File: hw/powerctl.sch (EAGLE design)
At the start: 12 parts, among them J1 MA02-1, J3 JST-XH-3P, J4 MA02-1

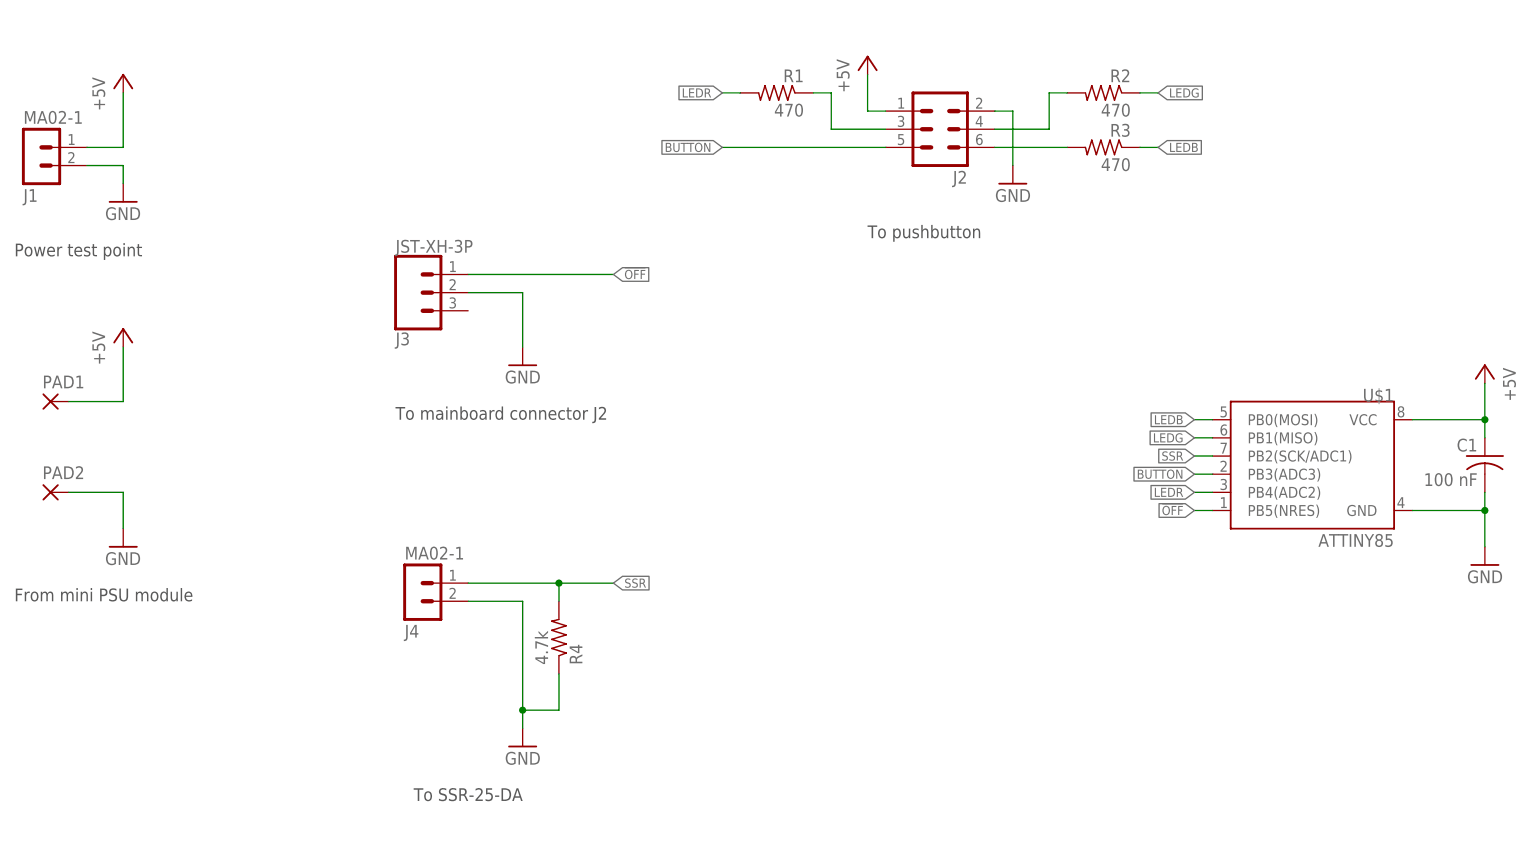
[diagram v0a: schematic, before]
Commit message: hw: update hardware, including warning about JST jumper cable
Update the hardware schematic to indicate the pinout for the button
connector, and note the oddness with the apparent commonness(???) of
JST jumper cable crossover cables.
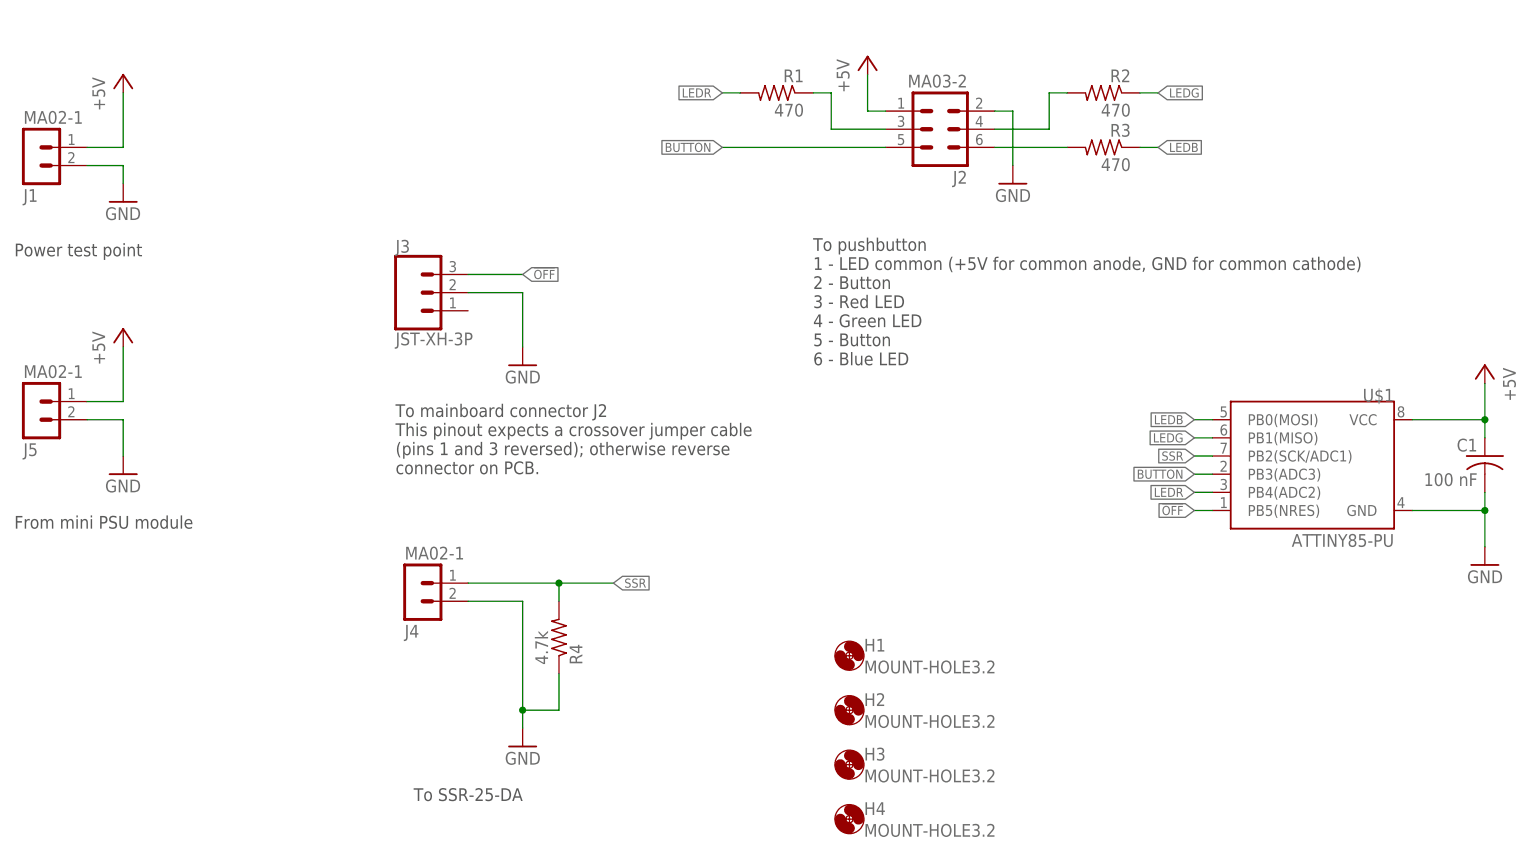
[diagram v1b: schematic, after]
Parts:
- removed PAD1, PAD2: (no value), wirepad:2,15/1,0
- added H1, H2, H3, H4: MOUNT-HOLE3.2, holes:MOUNT-HOLE3.2
- added J5: MA02-1, con-lstb:MA02-1
- J2: value (none) -> MA03-2
- U$1: value ATTINY85 -> ATTINY85-PU
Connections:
- net !OFF: now also J3.3; no longer J3.1
- net +5V: now also J5.1; no longer PAD1.P
- net GND: now also J5.2; no longer PAD2.P
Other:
- note added: "To mainboard connector J2 This pinout expects a crossover jumper cable (pins 1 and 3 reversed); otherwise reverse connector on PCB."
- note added: "To pushbutton 1 - LED common (+5V for common anode, GND for common cathode) 2 - Button 3 - Red LED 4 - Green LED 5 - Button 6 - Blue LED"
- note removed: "To mainboard connector J2"
- note removed: "To pushbutton"
- moved on the sheet: J3
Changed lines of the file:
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@@
 <parts>
 <part name="FRAME1" library="frames" deviceset="FRAME_A_L" device=""/>
-<part name="U$1" library="SparkFun" deviceset="ATTINY13" device="DIP" value="ATTINY85"/>
-<part name="PAD1" library="wirepad" deviceset="2,15/1,0" device=""/>
-<part name="PAD2" library="wirepad" deviceset="2,15/1,0" device=""/>
+<part name="U$1" library="SparkFun" deviceset="ATTINY13" device="DIP" value="ATTINY85-PU"/>
 <part name="P+1" library="supply1" deviceset="+5V" device=""/>
 <part name="GND1" library="supply1" deviceset="GND" device=""/>
@@
 <part name="J1" library="con-lstb" deviceset="MA02-1" device=""/>
 <part name="J4" library="con-lstb" deviceset="MA02-1" device=""/>
-<part name="J2" library="con-lstb" deviceset="MA03-2" device=""/>
+<part name="J2" library="con-lstb" deviceset="MA03-2" device="" value="MA03-2"/>
 <part name="P+4" library="supply1" deviceset="+5V" device=""/>
 <part name="GND6" library="supply1" deviceset="GND" device=""/>
@@
 <part name="P+5" library="supply1" deviceset="+5V" device=""/>
 <part name="GND8" library="supply1" deviceset="GND" device=""/>
+<part name="J5" library="con-lstb" deviceset="MA02-1" device=""/>
+<part name="H1" library="holes" deviceset="MOUNT-HOLE" device="3.2"/>
+<part name="H2" library="holes" deviceset="MOUNT-HOLE" device="3.2"/>
+<part name="H3" library="holes" deviceset="MOUNT-HOLE" device="3.2"/>
+<part name="H4" library="holes" deviceset="MOUNT-HOLE" device="3.2"/>
 </parts>
 <sheets>
 <sheet>
 <plain>
-<text x="30.48" y="104.14" size="1.778" layer="97">From mini PSU module</text>
+<text x="30.48" y="114.3" size="1.778" layer="97">From mini PSU module</text>
 <text x="30.48" y="152.4" size="1.778" layer="97">Power test point</text>
-<text x="149.86" y="154.94" size="1.778" layer="97">To pushbutton</text>
-<text x="83.82" y="129.54" size="1.778" layer="97">To mainboard connector J2</text>
+<text x="142.24" y="137.16" size="1.778" layer="97">To pushbutton
+1 - LED common (+5V for common anode, GND for common cathode)
+2 - Button
+3 - Red LED
+4 - Green LED
+5 - Button
+6 - Blue LED
+</text>
+<text x="83.82" y="121.92" size="1.778" layer="97">To mainboard connector J2
+This pinout expects a crossover jumper cable
+(pins 1 and 3 reversed); otherwise reverse
+connector on PCB.</text>
 <text x="86.36" y="76.2" size="1.778" layer="97">To SSR-25-DA</text>
 </plain>
@@
 <instance part="FRAME1" gate="G$2" x="172.72" y="0"/>
 <instance part="U$1" gate="G$1" x="210.82" y="121.92" rot="MR0"/>
-<instance part="PAD1" gate="1" x="35.56" y="132.08"/>
-<instance part="PAD2" gate="1" x="35.56" y="119.38"/>
 <instance part="P+1" gate="1" x="45.72" y="142.24"/>
-<instance part="GND1" gate="1" x="45.72" y="111.76"/>
+<instance part="GND1" gate="1" x="45.72" y="121.92"/>
 <instance part="P+2" gate="1" x="236.22" y="137.16" rot="MR0"/>
 <instance part="GND2" gate="1" x="236.22" y="109.22" rot="MR0"/>
@@
 <instance part="P+4" gate="1" x="149.86" y="180.34"/>
 <instance part="GND6" gate="1" x="170.18" y="162.56" rot="MR0"/>
-<instance part="J3" gate="J$1" x="86.36" y="147.32" rot="MR180"/>
+<instance part="J3" gate="J$1" x="86.36" y="147.32"/>
 <instance part="P+5" gate="1" x="45.72" y="177.8"/>
 <instance part="GND8" gate="1" x="45.72" y="160.02"/>
+<instance part="J5" gate="G$1" x="33.02" y="129.54" rot="MR180"/>
+<instance part="H1" gate="G$1" x="147.32" y="96.52"/>
+<instance part="H2" gate="G$1" x="147.32" y="88.9"/>
+<instance part="H3" gate="G$1" x="147.32" y="81.28"/>
+<instance part="H4" gate="G$1" x="147.32" y="73.66"/>
 </instances>
 <busses>
@@
 <net name="+5V" class="1">
 <segment>
-<pinref part="PAD1" gate="1" pin="P"/>
 <pinref part="P+1" gate="1" pin="+5V"/>
-<wire x1="38.1" y1="132.08" x2="45.72" y2="132.08" width="0.1524" layer="91"/>
+<wire x1="40.64" y1="132.08" x2="45.72" y2="132.08" width="0.1524" layer="91"/>
 <wire x1="45.72" y1="132.08" x2="45.72" y2="139.7" width="0.1524" layer="91"/>
+<pinref part="J5" gate="G$1" pin="1"/>
 </segment>
 <segment>
@@
 <net name="GND" class="1">
 <segment>
-<pinref part="PAD2" gate="1" pin="P"/>
 <pinref part="GND1" gate="1" pin="GND"/>
-<wire x1="38.1" y1="119.38" x2="45.72" y2="119.38" width="0.1524" layer="91"/>
-<wire x1="45.72" y1="119.38" x2="45.72" y2="114.3" width="0.1524" layer="91"/>
+<wire x1="45.72" y1="129.54" x2="45.72" y2="124.46" width="0.1524" layer="91"/>
+<pinref part="J5" gate="G$1" pin="2"/>
+<wire x1="45.72" y1="129.54" x2="40.64" y2="129.54" width="0.1524" layer="91"/>
 </segment>
 <segment>
@@
 </segment>
 <segment>
-<pinref part="J3" gate="J$1" pin="1"/>
-<wire x1="93.98" y1="149.86" x2="114.3" y2="149.86" width="0.1524" layer="91"/>
-<label x="114.3" y="149.86" size="1.27" layer="95" xref="yes"/>
+<pinref part="J3" gate="J$1" pin="3"/>
+<wire x1="93.98" y1="149.86" x2="101.6" y2="149.86" width="0.1524" layer="91"/>
+<label x="101.6" y="149.86" size="1.27" layer="95" xref="yes"/>
 </segment>
 </net>
@@
 </sheet>
 </sheets>
+<errors>
+</errors>
 </schematic>
 </drawing>
+<compatibility>
+<note version="6.3" minversion="6.2.2" severity="warning">
+Since Version 6.2.2 text objects can contain more than one line,
+which will not be processed correctly with this version.
+</note>
+</compatibility>
 </eagle>
